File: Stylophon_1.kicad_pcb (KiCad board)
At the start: 2 copper layers, 57 x 38.5 mm, 71 parts, among them J1 Conn_01x02_Socket, J2 +, J3 -, J4 Stylus, SW1 On/Off, SW2 Vibrato, T1 BC846, T2 BC846, U1 NE555D

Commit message: PCB updated
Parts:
- removed J2: +, Connector_PinHeader_2.00mm:PinHeader_1x01_P2.00mm_Vertical
- removed J3: -, Connector_PinHeader_2.00mm:PinHeader_1x01_P2.00mm_Vertical
- added BT1: Battery, Connector_PinHeader_2.54mm:PinHeader_1x02_P2.54mm_Vertical, B.Cu at (88.4, 115.2)
- C1, C2, C3, C4: value 0,1uF -> 100nF
- C6: value 27nF -> 33nF
- D1: value 1S44 -> LL4148
- J1, J4, LS1: moved to B.Cu
- R21, R24: value 68k -> 56K
- R22: value 10M -> 1,8M
- R23: value 58k -> 56K
- R28: value 680 -> 680R
- R29: value 4,7k -> 4k7
- R30: value 56 -> 68R
- RV1: value 4k7 -> 50k; moved to B.Cu
- RV2: value 220 -> 1K; moved to B.Cu
- TP1, TP10, TP11, TP12, TP13, TP14, TP15, TP16, TP17, TP18, TP19, TP2, TP20, TP3, TP4, TP5, TP6, TP7, TP8, TP9: footprint TestPoint:TestPoint_Pad_4.0x4.0mm -> Keypads:Keypad_Small
- moved R31 42.9 mm to (88.5, 128.5)
- moved C2 6.18 mm to (113.5, 110.0), turned to 90 degrees
- moved R23 6.18 mm to (113.5, 114.5)
- moved TP4 5.15 mm to (133.0, 134.0)
- moved TP17 4.92 mm to (98.5, 138.5)
- moved TP16 4.74 mm to (100.5, 134.0)
- moved TP9 4.74 mm to (118.5, 134.0)
- moved TP11 4.61 mm to (113.5, 134.0)
- moved TP12 4.61 mm to (112.0, 138.5)
- moved TP5 4.53 mm to (130.0, 138.5)
- moved TP10 4.50 mm to (116.5, 138.5)
- moved RV2 4.00 mm to (133.5, 119.5)
- moved R17 3.43 mm to (99.4, 128.5)
- moved R18 3.20 mm to (96.7, 128.5)
- moved R16 3.16 mm to (102.2, 128.5)
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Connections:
- net Net-(J2-Pin_1) renamed +9V
- net Net-(R1-Pad2) renamed /12
- net Net-(R10-Pad1) renamed /7,5
- net Net-(R10-Pad2) renamed /7
- net Net-(R11-Pad2) renamed /6,5
- net Net-(R12-Pad2) renamed /6
- net Net-(R13-Pad2) renamed /5
- net Net-(R14-Pad2) renamed /4,5
- net Net-(R15-Pad2) renamed /4
- net Net-(R16-Pad2) renamed /3,5
- net Net-(R17-Pad2) renamed /3
- net Net-(R18-Pad2) renamed /2
- net Net-(R19-Pad2) renamed /1,5
- net Net-(R2-Pad2) renamed /11,5
- net Net-(R20-Pad2) renamed /1
- net Net-(R3-Pad2) renamed /11
- net Net-(R4-Pad2) renamed /10,5
- net Net-(R5-Pad2) renamed /10
- net Net-(R6-Pad2) renamed /9
- net Net-(R7-Pad2) renamed /8,5
- net Net-(R8-Pad2) renamed /8
- C5 pad 2: Net-(J1-Pin_1) -> GND
- C6 pad 2: Net-(J1-Pin_1) -> GND
- J1 pad 1: Net-(J1-Pin_1) -> GND
- LS1 pad 1: Net-(J1-Pin_2) -> GND
- LS1 pad 2: Net-(J1-Pin_1) -> Net-(J1-Pin_2)
- R23 pad 2: Net-(J1-Pin_1) -> GND
- R24 pad 2: Net-(J1-Pin_1) -> GND
- R26 pad 2: Net-(J1-Pin_1) -> GND
- R31 pad 2: Net-(J1-Pin_1) -> GND
- RV2 pad 1: Net-(C7-Pad2) -> GND
- RV2 pad 3: Net-(J1-Pin_1) -> Net-(C7-Pad2)
- SW1 pad 2: Net-(J1-Pin_1) -> GND
- SW2 pad 1: Net-(J1-Pin_1) -> GND
- T1 pad 2: Net-(J1-Pin_1) -> GND
- U1 pad 1: Net-(J1-Pin_1) -> GND
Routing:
- net Net-(J1-Pin_1): track 84.7 -> 0.00 mm, vias 2 -> 0
- net GND: track 0.00 -> 78.3 mm, vias 0 -> 2
- net /1: track 57.8 -> 13.1 mm
- net Net-(T1-C): track 42.7 -> 35.4 mm
- net Net-(C2-Pad1): track 10.7 -> 3.91 mm
- net /6: track 8.71 -> 14.1 mm
- net Net-(D1-A): track 11.5 -> 6.33 mm
- net /7: track 9.18 -> 14.4 mm
- net /10: track 8.50 -> 13.6 mm
- net /3: track 8.29 -> 13.4 mm
- net /10,5: track 13.9 -> 8.95 mm
- net /6,5: track 13.9 -> 9.14 mm
- net /7,5: track 13.7 -> 9.29 mm
- net /3,5: track 13.2 -> 8.85 mm
- net Net-(T1-B): track 8.57 -> 4.80 mm
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- added copper zone on B.Cu, net GND
- added copper zone on F.Cu, net GND

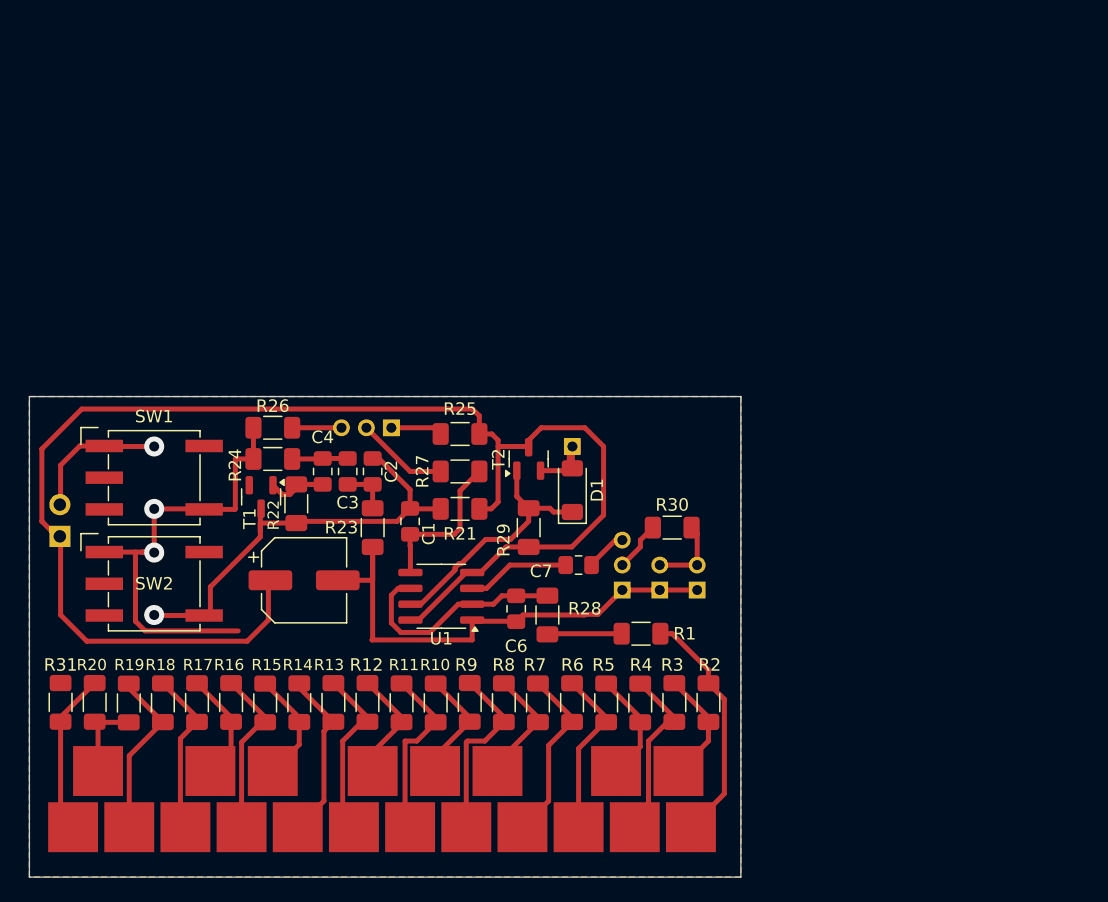
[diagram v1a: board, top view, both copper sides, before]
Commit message: Added keys like a real one
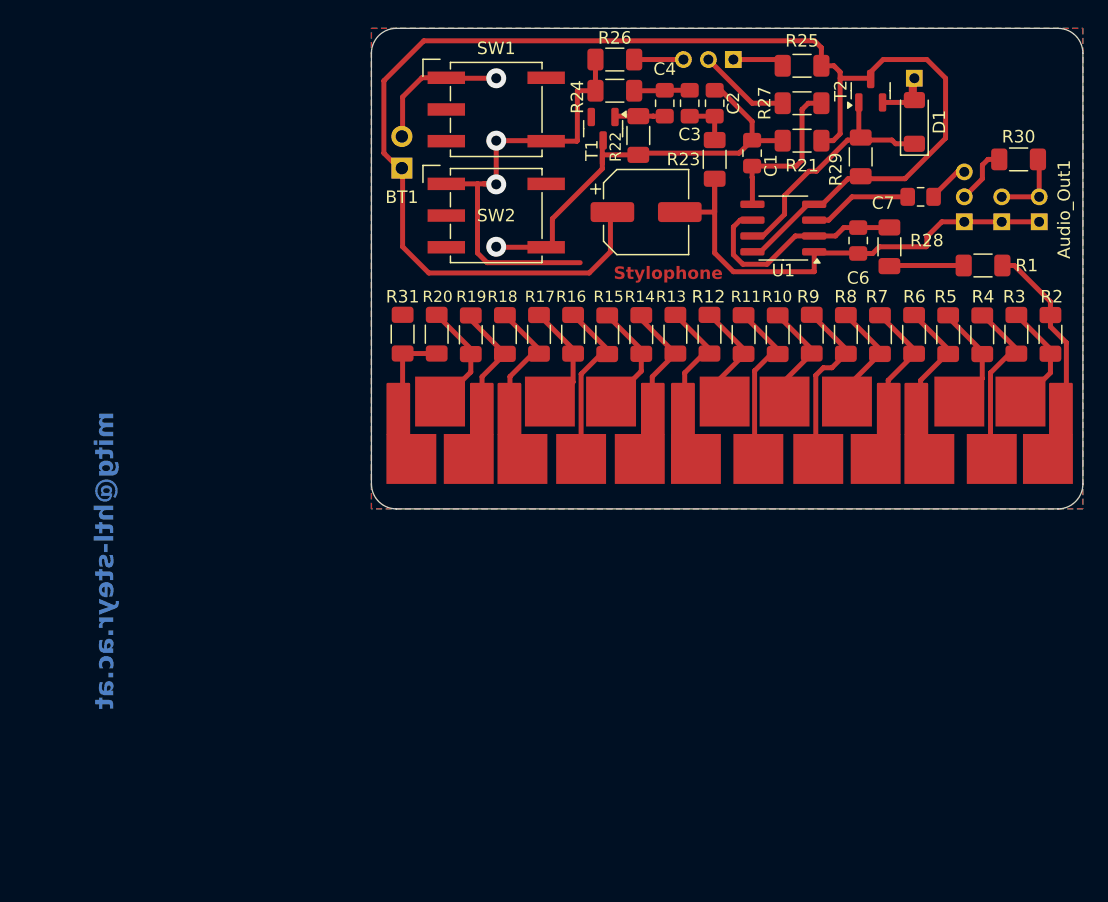
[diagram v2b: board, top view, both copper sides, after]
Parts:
- BT1: value Battery -> 9V
- LS1: value 75Ohm -> 300R
- TP1, TP13, TP18, TP6: footprint Keypads:Keypad_Small -> Keypads:Keypad_Right
- TP12, TP17, TP20, TP5: footprint Keypads:Keypad_Small -> Keypads:Keypad_Left
- moved TP1 41.2 mm to (167.8, 109.0)
- moved TP3 41.1 mm to (163.1, 109.0)
- moved TP6 41.0 mm to (154.0, 109.0)
- moved TP11 40.9 mm to (141.7, 104.4)
- moved TP8 40.8 mm to (149.2, 109.0)
- moved TP7 40.7 mm to (151.5, 104.4)
- moved TP9 40.7 mm to (146.5, 104.4)
- moved TP5 40.7 mm to (158.1, 109.0)
- moved TP10 40.6 mm to (144.4, 109.0)
- moved R30 40.5 mm to (165.2, 85.0)
- moved TP4 40.4 mm to (160.5, 104.4)
- moved TP13 40.4 mm to (135.1, 109.0)
- moved TP19 40.3 mm to (118.9, 104.4)
- moved TP2 40.3 mm to (165.4, 104.4)
- moved R14 40.3 mm to (135.0, 99.0)
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- renumbered J1 to Audio_Out1
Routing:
- net /1,5: track 6.81 -> 8.46 mm
- net /3: track 13.4 -> 15.0 mm
- net /1: track 13.1 -> 12.4 mm
- net Net-(U1-CV): track 12.5 -> 13.1 mm
- net /7: track 14.4 -> 13.8 mm
- net GND: track 78.3 -> 77.8 mm
- net Net-(D1-K): track 20.8 -> 21.3 mm
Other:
- outline, holes or cut-outs redrawn
- board text added: "Stylophone"
- board text added: "mitg@htl-steyr.ac.at"
